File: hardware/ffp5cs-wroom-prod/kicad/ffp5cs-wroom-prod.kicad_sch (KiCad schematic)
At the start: 67 parts, among them J1 Bornier_5.08, J10 JST-XH, J11 Bornier_5.08, J12 Bornier_5.08, J13 Support OLED, J14 Support I2C ext, J15 Header servo, J16 Header servo, J17 Header GPIO libres, J2 Jack 5.5/2.1, J3 Bornier_5.08, J4 Bornier_5.08, J5 Bornier_5.08, J6 Bornier_5.08, J7 JST-XH, J8 JST-XH, J9 JST-XH, K1 SRD-05VDC-SL-C, K2 SRD-05VDC-SL-C, K3 SRD-05VDC-SL-C, K4 SRD-05VDC-SL-C, Q1 BC337-40, Q2 BC337-40, Q3 BC337-40, Q4 BC337-40

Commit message: hardware(ffp5cs): 3 ports I2C libres par carte + pipeline de routage LV scripté
Demande : pouvoir brancher des modules I2C supplémentaires sans soudure.
Avec les pull-ups 4.7k en place, 3-4 modules simultanés sont confortables
(limite = capacité du bus, pas l'ESP) — dimensionné en conséquence :

- 12/24V (rev 0.4) : +J18 +J19 (supports 1x4 GND/VCC/SCL/SDA, mêmes nets
  que J14) ; netclasses Relais/Alim désormais émises par generate.py ;
  nouveau generator/route_lv.py (pipeline scripté dérivé de route_230v.py :
  freerouting, vias de couture, îlots supprimés, reliefs corrigés, bandes
  de bord) ; re-routage complet, gerbers v0.4 (remplacent v0.3).
- 230V (rev 0.2) : +J21 +J22 idem ; bandes de keepout le long des bords
  ajoutées au pipeline (l'autorouteur frôlait l'edge clearance) ;
  re-routage complet, gerbers v0.2 (remplacent v0.1).
- Validation des DEUX cartes : ERC 0 erreur, DRC 0 violation, 0 pad non
  connecté, contrôle 3mm secteur/logique (230V) : 0 écart, checker
  pins.h <-> schéma <-> PCB vert.
- READMEs : ports I2C documentés (3-4 modules max, bus < ~50cm, sinon
  pull-ups 2.2k).

Co-Authored-By: Claude Fable 5 <noreply@anthropic.com>
Claude-Session: https://claude.ai/code/session_01HcxShQb65yktRwp31wBq9q
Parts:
- added J18, J19: Support I2C libre, ffp5cs:PinSocket_1x04_P2.54mm_Vertical, symbol ffp5cs:CONN_04
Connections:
- net +3V3: now also J18.2, J19.2
- net GND: now also J18.1, J19.1
- net I2C_SCL_GPIO22: now also J18.3, J19.3
- net I2C_SDA_GPIO21: now also J18.4, J19.4
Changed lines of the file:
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@@
     (title "ffp5cs wroom-prod - carte porteuse ESP32 DevKit V1")
     (date "2026-07-07")
-    (rev "0.1")
+    (rev "0.4")
     (company "salle aeree n3")
     (comment 1 "Genere par hardware/ffp5cs-wroom-prod/generator/generate.py")
@@
     (effects (font (size 1.27 1.27)) (justify left bottom))
 )
+  (symbol (lib_id "ffp5cs:CONN_04") (at 264.16 254.00 0) (unit 1)
+    (exclude_from_sim no) (in_bom yes) (on_board yes) (dnp no)
+    (property "Reference" "J18" (at 264.16 243.84 0) (effects (font (size 1.27 1.27))))
+    (property "Value" "Support I2C libre" (at 264.16 245.98 0) (effects (font (size 1.27 1.27))))
+    (property "Footprint" "ffp5cs:PinSocket_1x04_P2.54mm_Vertical" (at 264.16 254.00 0) (effects (font (size 1.27 1.27)) (hide yes)))
+    (property "Datasheet" "~" (at 264.16 254.00 0) (effects (font (size 1.27 1.27)) (hide yes)))
+    (property "Description" "Port I2C libre 2 (1=GND 2=VCC 3=SCL 4=SDA)" (at 264.16 254.00 0) (effects (font (size 1.27 1.27)) (hide yes)))
+    (pin "1")
+    (pin "2")
+    (pin "3")
+    (pin "4")
+    (instances (project "ffp5cs-wroom-prod" (path "/8cd84e2d-c95e-5adb-846f-a905f327881a" (reference "J18") (unit 1))))
+  )
+  (wire (pts (xy 257.81 248.92) (xy 255.27 248.92))
+    (stroke (width 0) (type default)))
+  (label "GND" (at 255.27 248.92 0)
+    (effects (font (size 1.27 1.27)) (justify right bottom))
+)
+  (wire (pts (xy 257.81 251.46) (xy 255.27 251.46))
+    (stroke (width 0) (type default)))
+  (label "+3V3" (at 255.27 251.46 0)
+    (effects (font (size 1.27 1.27)) (justify right bottom))
+)
+  (wire (pts (xy 257.81 254.00) (xy 255.27 254.00))
+    (stroke (width 0) (type default)))
+  (label "I2C_SCL_GPIO22" (at 255.27 254.00 0)
+    (effects (font (size 1.27 1.27)) (justify right bottom))
+)
+  (wire (pts (xy 257.81 256.54) (xy 255.27 256.54))
+    (stroke (width 0) (type default)))
+  (label "I2C_SDA_GPIO21" (at 255.27 256.54 0)
+    (effects (font (size 1.27 1.27)) (justify right bottom))
+)
+  (symbol (lib_id "ffp5cs:CONN_04") (at 264.16 274.32 0) (unit 1)
+    (exclude_from_sim no) (in_bom yes) (on_board yes) (dnp no)
+    (property "Reference" "J19" (at 264.16 264.16 0) (effects (font (size 1.27 1.27))))
+    (property "Value" "Support I2C libre" (at 264.16 266.30 0) (effects (font (size 1.27 1.27))))
+    (property "Footprint" "ffp5cs:PinSocket_1x04_P2.54mm_Vertical" (at 264.16 274.32 0) (effects (font (size 1.27 1.27)) (hide yes)))
+    (property "Datasheet" "~" (at 264.16 274.32 0) (effects (font (size 1.27 1.27)) (hide yes)))
+    (property "Description" "Port I2C libre 3 (1=GND 2=VCC 3=SCL 4=SDA)" (at 264.16 274.32 0) (effects (font (size 1.27 1.27)) (hide yes)))
+    (pin "1")
+    (pin "2")
+    (pin "3")
+    (pin "4")
+    (instances (project "ffp5cs-wroom-prod" (path "/8cd84e2d-c95e-5adb-846f-a905f327881a" (reference "J19") (unit 1))))
+  )
+  (wire (pts (xy 257.81 269.24) (xy 255.27 269.24))
+    (stroke (width 0) (type default)))
+  (label "GND" (at 255.27 269.24 0)
+    (effects (font (size 1.27 1.27)) (justify right bottom))
+)
+  (wire (pts (xy 257.81 271.78) (xy 255.27 271.78))
+    (stroke (width 0) (type default)))
+  (label "+3V3" (at 255.27 271.78 0)
+    (effects (font (size 1.27 1.27)) (justify right bottom))
+)
+  (wire (pts (xy 257.81 274.32) (xy 255.27 274.32))
+    (stroke (width 0) (type default)))
+  (label "I2C_SCL_GPIO22" (at 255.27 274.32 0)
+    (effects (font (size 1.27 1.27)) (justify right bottom))
+)
+  (wire (pts (xy 257.81 276.86) (xy 255.27 276.86))
+    (stroke (width 0) (type default)))
+  (label "I2C_SDA_GPIO21" (at 255.27 276.86 0)
+    (effects (font (size 1.27 1.27)) (justify right bottom))
+)
   (symbol (lib_id "ffp5cs:CONN_10") (at 60.96 172.72 0) (unit 1)

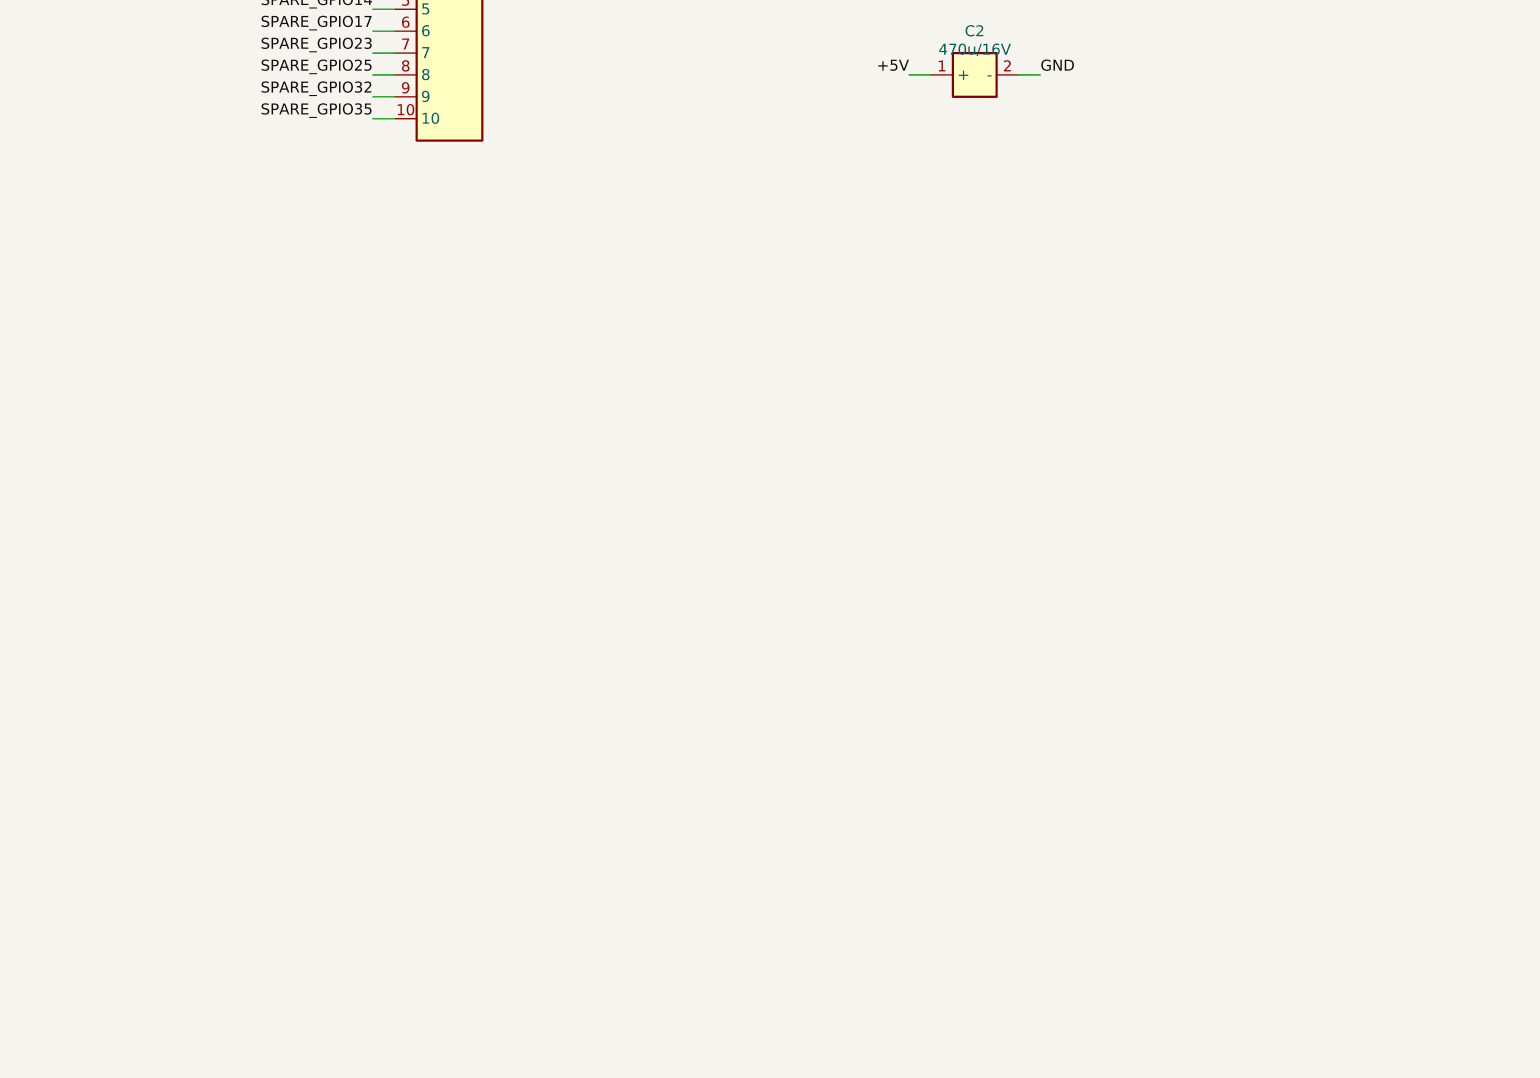
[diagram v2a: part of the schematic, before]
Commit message: feat(hardware+ffp5cs): carte 12/24V bi-module — site A2 ESP32-S3-DevKitC-1 (rev 0.6, firmware v15.27)
Option A : la carte porteuse ffp5cs-wroom-prod accueille au choix un DevKit V1
WROOM (site A1, 2x15) ou un ESP32-S3-DevKitC-1 (site A2, 2x22) — un seul module
peuplé. Chaque net fonctionnel touche les deux sites ; carte agrandie 150x100 ->
190x100 mm, header J20 = breakout GPIO S3 (AUX1=IO47, AUX2=IO42).

Firmware v15.27 : nouvelle cartographie Pins « carrier » sélectionnée par
-DPINMAP_S3_CARRIER (env wroom-s3-carrier-test, ajouté à la CI). La cartographie
S3 historique (système câblé main en production) est INCHANGÉE. Corrections
intégrées au carrier : ONE_WIRE 37->41 (PSRAM octale), ULTRASON_POTA 45->5 et
LUMINOSITE 3->1 (strapping), AUX2 48->42 (LED RGB du DevKitC-1).

Pipeline : generate.py (symbole+empreinte S3 44p, keepout antenne A2),
route_lv.py (SEED_TRACKS pads pincés/rives encombrées + VIA_BLOCKS anti-court
freerouting), tidy_silkscreen, export_fab. Validations : ERC 0, DRC 0/0/0,
garde anti-dérive 16+16 signaux (2 sites, broches S3 interdites vérifiées),
zip fab 10 fichiers (PTH 367 + NPTH 4), builds wroom-test / wroom-s3-test /
wroom-s3-carrier-test SUCCESS.

Co-Authored-By: Claude <noreply@anthropic.com>
Claude-Session: https://claude.ai/code/session_01HcxShQb65yktRwp31wBq9q
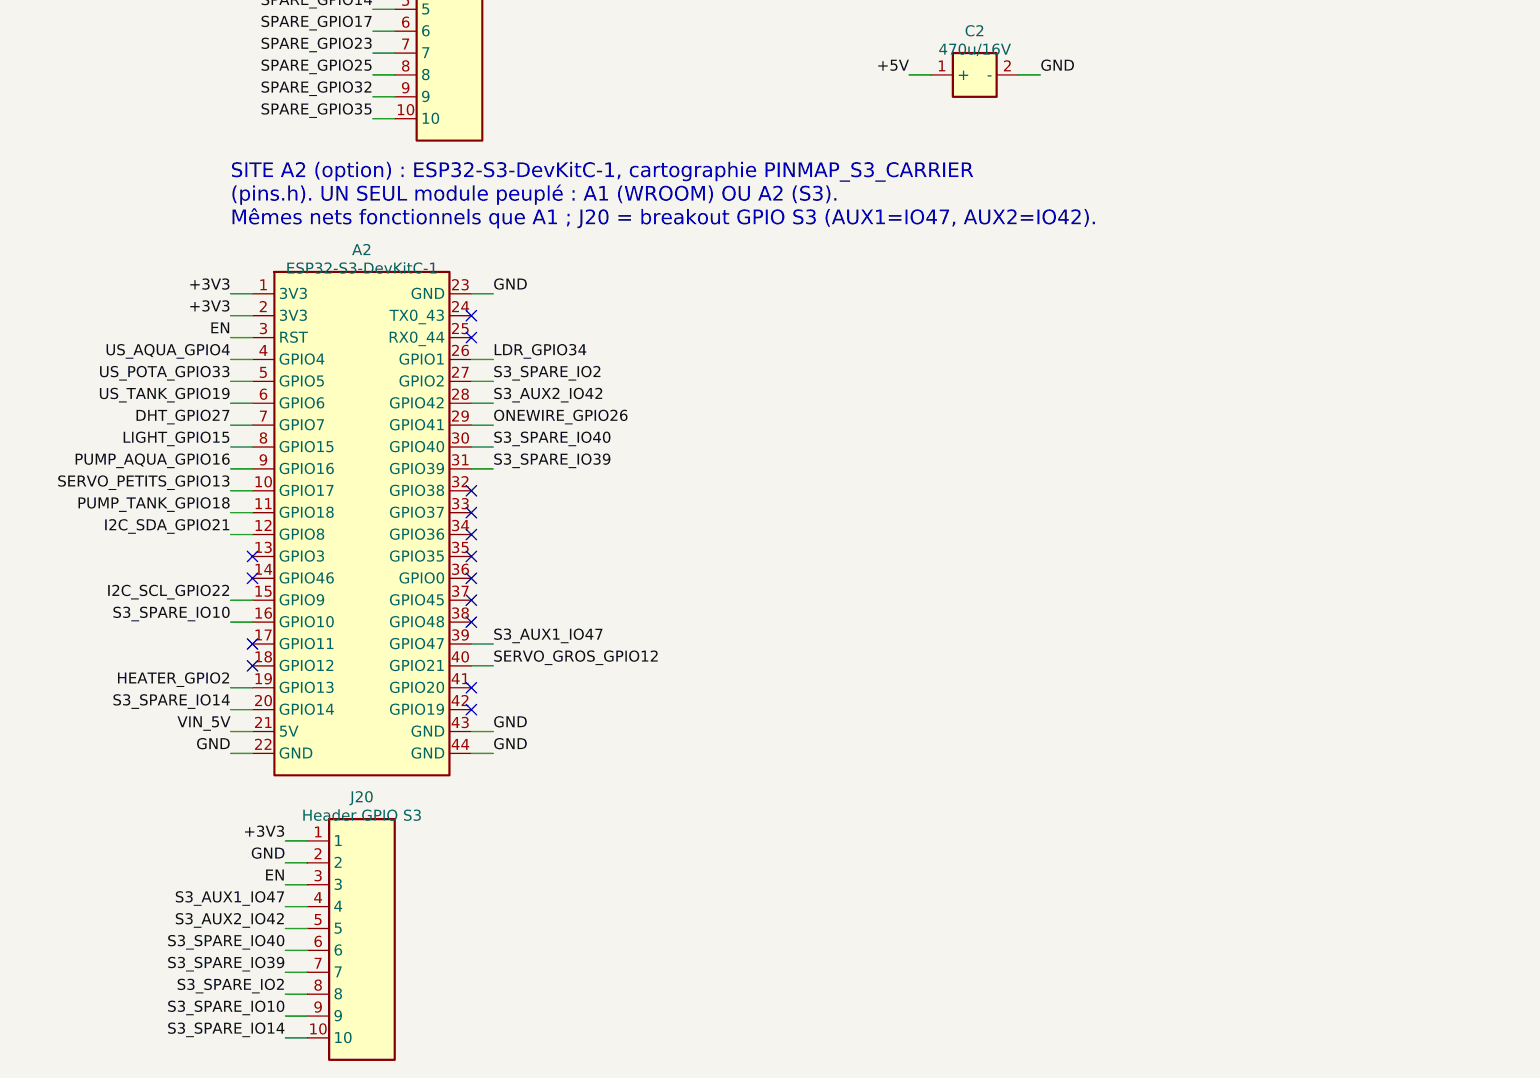
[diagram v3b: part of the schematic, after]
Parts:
- added A2: ESP32-S3-DevKitC-1, ffp5cs:ESP32_S3_DevKitC_1_44pin, symbol ffp5cs:ESP32_S3_DEVKITC_44
- added J20: Header GPIO S3, ffp5cs:PinHeader_1x10_P2.54mm_Vertical, symbol ffp5cs:CONN_10
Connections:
- net +3V3: now also A2.1 (3V3), A2.2 (3V3), J20.1
- net DHT_GPIO27: now also A2.7 (GPIO7)
- net EN: now also A2.3 (RST), J20.3
- net GND: now also A2.22 (GND), A2.23 (GND), A2.43 (GND), A2.44 (GND), J20.2
- net HEATER_GPIO2: now also A2.19 (GPIO13)
- net I2C_SCL_GPIO22: now also A2.15 (GPIO9)
- net I2C_SDA_GPIO21: now also A2.12 (GPIO8)
- net LDR_GPIO34: now also A2.26 (GPIO1)
- net LIGHT_GPIO15: now also A2.8 (GPIO15)
- net ONEWIRE_GPIO26: now also A2.29 (GPIO41)
- net PUMP_AQUA_GPIO16: now also A2.9 (GPIO16)
- net PUMP_TANK_GPIO18: now also A2.11 (GPIO18)
- net SERVO_GROS_GPIO12: now also A2.40 (GPIO21)
- net SERVO_PETITS_GPIO13: now also A2.10 (GPIO17)
- net US_AQUA_GPIO4: now also A2.4 (GPIO4)
- net US_POTA_GPIO33: now also A2.5 (GPIO5)
- net US_TANK_GPIO19: now also A2.6 (GPIO6)
- net VIN_5V: now also A2.21 (5V)
- new net S3_AUX1_IO47: A2.39 (GPIO47), J20.4
- new net S3_AUX2_IO42: A2.28 (GPIO42), J20.5
- new net S3_SPARE_IO10: A2.16 (GPIO10), J20.9
- new net S3_SPARE_IO14: A2.20 (GPIO14), J20.10
- new net S3_SPARE_IO2: A2.27 (GPIO2), J20.8
- new net S3_SPARE_IO39: A2.31 (GPIO39), J20.7
- new net S3_SPARE_IO40: A2.30 (GPIO40), J20.6
- no-connect marks 4 -> 19
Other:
- note added: "SITE A2 (option) : ESP32-S3-DevKitC-1, cartographie PINMAP_S3_CARRIER (pins.h). UN SEUL module peuplé : A1 (WROOM) OU A2 (S3). Mêmes nets fonctionnels que A1 ; J20 = breakout GPIO S3 (AUX1=IO47, AUX2=IO42)."
- title: ffp5cs wroom-prod - carte porteuse ESP32 DevKit V1 -> ffp5cs wroom-prod - carte porteuse bi-module ESP32 (DevKit V1 / S3-DevKitC-1)
